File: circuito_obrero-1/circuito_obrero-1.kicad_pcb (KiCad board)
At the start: 2 copper layers, 13 parts, among them J1 Conn_01x03_Pin, J10 Conn_01x05, J2 Conn_01x03_Pin, J3 Conn_01x03_Pin, J4 Conn_01x03_Pin, J5 Conn_01x03_Pin, J6 Conn_01x03_Pin, J7 Conn_01x03_Pin, J8 Conn_01x03_Pin, J9 Conn_01x05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

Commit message: agregadas las resis al circuito
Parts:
- added R1: R, Resistor_THT:R_Axial_DIN0204_L3.6mm_D1.6mm_P5.08mm_Horizontal, F.Cu at (105.5, 89.1)
- added R10: R, Resistor_THT:R_Axial_DIN0204_L3.6mm_D1.6mm_P5.08mm_Horizontal, F.Cu at (113.5, 89.1)
- added R11: R, Resistor_THT:R_Axial_DIN0204_L3.6mm_D1.6mm_P5.08mm_Horizontal, F.Cu at (113.5, 92.2)
- added R12: R, Resistor_THT:R_Axial_DIN0204_L3.6mm_D1.6mm_P5.08mm_Horizontal, F.Cu at (113.5, 95.4)
- added R13: R, Resistor_THT:R_Axial_DIN0204_L3.6mm_D1.6mm_P5.08mm_Horizontal, F.Cu at (113.5, 98.5)
- added R14: R, Resistor_THT:R_Axial_DIN0204_L3.6mm_D1.6mm_P5.08mm_Horizontal, F.Cu at (113.5, 101.7)
- added R15: R, Resistor_THT:R_Axial_DIN0204_L3.6mm_D1.6mm_P5.08mm_Horizontal, F.Cu at (113.5, 104.8)
- added R16: R, Resistor_THT:R_Axial_DIN0204_L3.6mm_D1.6mm_P5.08mm_Horizontal, F.Cu at (113.5, 108.0)
- added R17: R, Resistor_THT:R_Axial_DIN0204_L3.6mm_D1.6mm_P5.08mm_Horizontal, F.Cu at (113.5, 111.1)
- added R18: R, Resistor_THT:R_Axial_DIN0204_L3.6mm_D1.6mm_P5.08mm_Horizontal, F.Cu at (113.5, 114.3)
- added R19: R, Resistor_THT:R_Axial_DIN0204_L3.6mm_D1.6mm_P5.08mm_Horizontal, F.Cu at (153.0, 85.5)
- added R2: R, Resistor_THT:R_Axial_DIN0204_L3.6mm_D1.6mm_P5.08mm_Horizontal, F.Cu at (105.5, 92.2)
- added R20: R, Resistor_THT:R_Axial_DIN0204_L3.6mm_D1.6mm_P5.08mm_Horizontal, F.Cu at (153.0, 81.5)
- added R21: R, Resistor_THT:R_Axial_DIN0204_L3.6mm_D1.6mm_P5.08mm_Horizontal, F.Cu at (121.5, 95.4)
- added R22: R, Resistor_THT:R_Axial_DIN0204_L3.6mm_D1.6mm_P5.08mm_Horizontal, F.Cu at (143.9, 77.5)
- added R23: R, Resistor_THT:R_Axial_DIN0204_L3.6mm_D1.6mm_P5.08mm_Horizontal, F.Cu at (121.5, 101.7)
- added R24: R, Resistor_THT:R_Axial_DIN0204_L3.6mm_D1.6mm_P5.08mm_Horizontal, F.Cu at (121.5, 104.8)
- added R3: R, Resistor_THT:R_Axial_DIN0204_L3.6mm_D1.6mm_P5.08mm_Horizontal, F.Cu at (105.5, 95.4)
- added R4: R, Resistor_THT:R_Axial_DIN0204_L3.6mm_D1.6mm_P5.08mm_Horizontal, F.Cu at (105.5, 98.5)
- added R5: R, Resistor_THT:R_Axial_DIN0204_L3.6mm_D1.6mm_P5.08mm_Horizontal, F.Cu at (105.5, 101.7)
- added R6: R, Resistor_THT:R_Axial_DIN0204_L3.6mm_D1.6mm_P5.08mm_Horizontal, F.Cu at (105.5, 104.8)
- added R7: R, Resistor_THT:R_Axial_DIN0204_L3.6mm_D1.6mm_P5.08mm_Horizontal, F.Cu at (105.5, 108.0)
- added R8: R, Resistor_THT:R_Axial_DIN0204_L3.6mm_D1.6mm_P5.08mm_Horizontal, F.Cu at (105.5, 111.1)
- added R9: R, Resistor_THT:R_Axial_DIN0204_L3.6mm_D1.6mm_P5.08mm_Horizontal, F.Cu at (105.5, 114.3)
- moved J10 116.3 mm to (193.0, 60.5), turned to -90 degrees
- moved J8 111.9 mm to (176.0, 71.0), turned to 90 degrees
- moved U3 54.4 mm to (152.4, 59.4)
- moved J9 40.1 mm to (40.0, 53.5), turned to -90 degrees
- moved U2 30.8 mm to (118.4, 49.8)
- moved U1 21.2 mm to (96.7, 51.9)
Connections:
- J10 pad 4: VCC -> GND
- J9 pad 4: VCC -> GND

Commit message: vcc funcional
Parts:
- moved J6 96.1 mm to (161.5, 74.3), turned to 180 degrees
- moved R24 74.9 mm to (190.4, 75.4), turned to 90 degrees
- moved J7 74.9 mm to (140.0, 88.8), turned to -90 degrees
- moved R23 70.8 mm to (187.3, 75.4), turned to 90 degrees
- moved J1 67.9 mm to (114.7, 93.8), turned to 90 degrees
- moved R21 62.7 mm to (181.0, 75.4), turned to 90 degrees
- moved R18 60.9 mm to (174.4, 113.3)
- moved J5 60.2 mm to (125.5, 73.8)
- moved J4 59.5 mm to (123.5, 52.0), turned to 180 degrees
- moved R9 58.3 mm to (106.5, 56.0), turned to 90 degrees
- moved R12 53.2 mm to (144.0, 51.8), turned to 90 degrees
- moved R17 51.4 mm to (164.4, 103.8)
- moved R16 50.0 mm to (146.5, 70.4), turned to 90 degrees
- moved R11 48.8 mm to (140.8, 51.8), turned to 90 degrees
- moved R10 44.4 mm to (137.7, 51.8), turned to 90 degrees
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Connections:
- J10 pad 4: GND -> VCC
- J9 pad 4: GND -> VCC
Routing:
- net (no net): track 0.00 -> 692.0 mm
- net GND: track 0.00 -> 10.1 mm

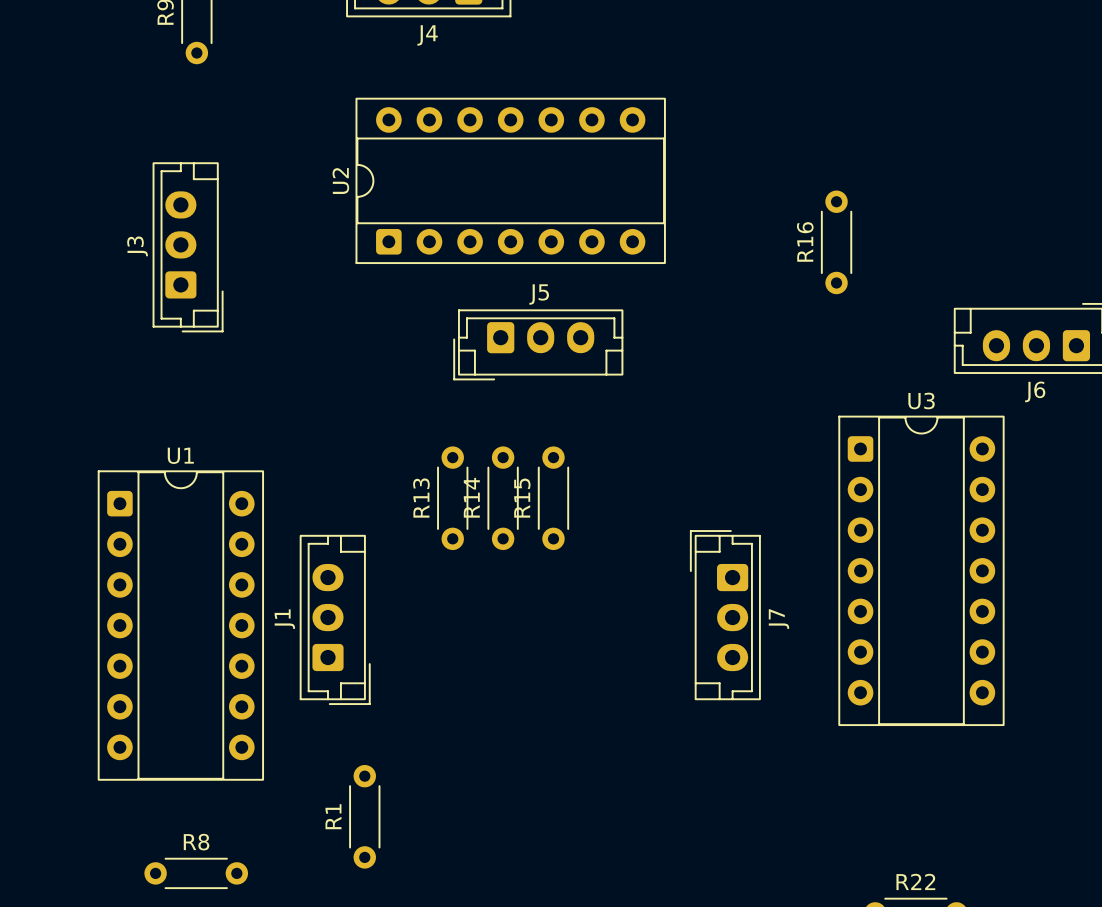
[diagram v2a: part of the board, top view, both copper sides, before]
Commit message: acomodando resistencias (revisar si es pull up o pull down el btn y los encoders)
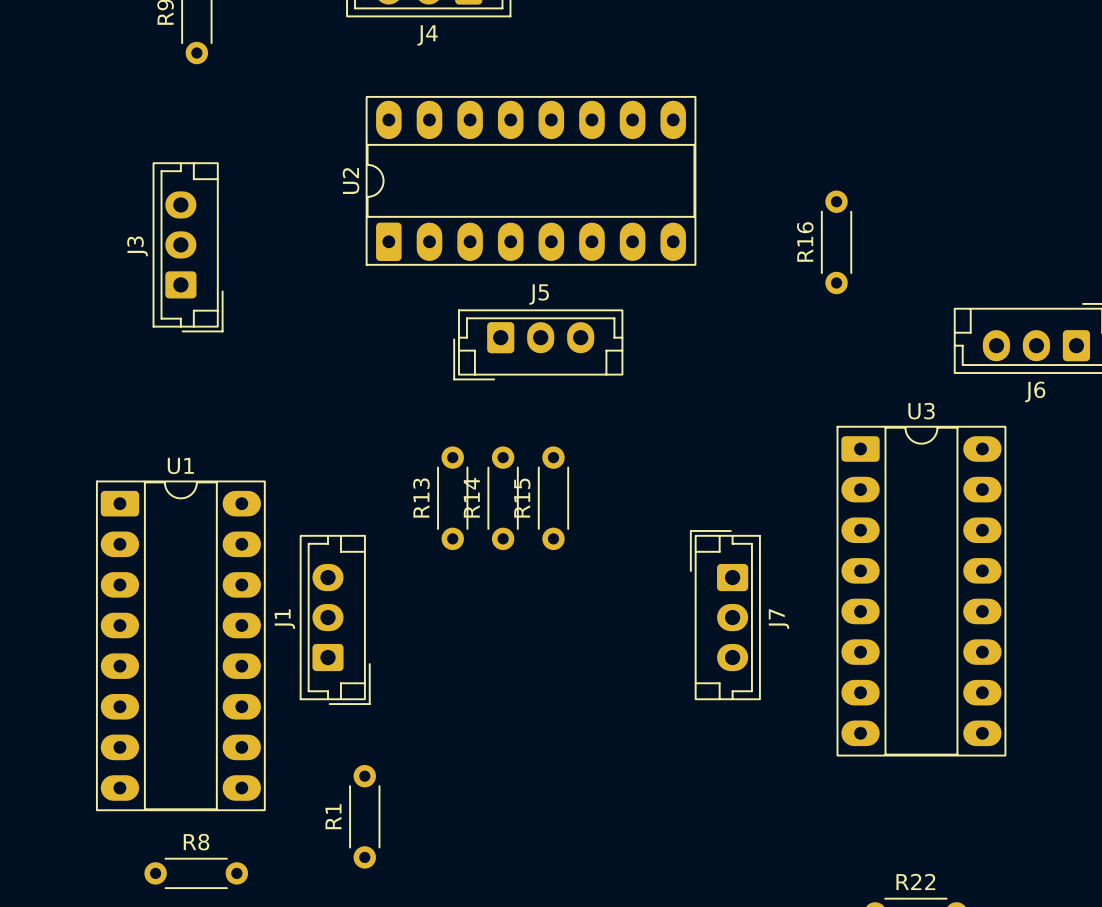
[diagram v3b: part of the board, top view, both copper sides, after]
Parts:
- U1, U2, U3: footprint Package_DIP:CERDIP-14_W7.62mm_SideBrazed_Socket -> Package_DIP:CERDIP-16_W7.62mm_SideBrazed_LongPads_Socket
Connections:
- R1 pad 1: GND -> VCC
- R10 pad 1: GND -> VCC
- R11 pad 1: Net-(J4-Pin_2) -> GND
- R11 pad 2: unconnected-(R11-Pad2) -> Net-(J4-Pin_2)
- R12 pad 1: GND -> VCC
- R13 pad 1: Net-(J5-Pin_1) -> VCC
- R13 pad 2: unconnected-(R13-Pad2) -> Net-(J5-Pin_1)
- R14 pad 1: Net-(J5-Pin_2) -> GND
- R14 pad 2: unconnected-(R14-Pad2) -> Net-(J5-Pin_2)
- R15 pad 2: unconnected-(R15-Pad2) -> VCC
- R16 pad 2: GND -> VCC
- R18 pad 1: GND -> VCC
- R19 pad 1: Net-(J7-Pin_3) -> VCC
- R19 pad 2: GND -> Net-(J6-Pin_1)
- R20 pad 1: Net-(J7-Pin_2) -> GND
- R20 pad 2: GND -> Net-(J6-Pin_2)
- R21 pad 1: GND -> VCC
- R21 pad 2: Net-(J7-Pin_1) -> Net-(J6-Pin_3)
- R22 pad 1: Net-(J6-Pin_3) -> VCC
- R22 pad 2: GND -> Net-(J7-Pin_1)
- R23 pad 1: Net-(J6-Pin_2) -> GND
- R23 pad 2: GND -> Net-(J7-Pin_2)
- R24 pad 1: GND -> VCC
- R24 pad 2: Net-(J6-Pin_1) -> Net-(J7-Pin_3)
- R3 pad 1: GND -> VCC
- R4 pad 1: GND -> VCC
- R6 pad 1: GND -> VCC
- R7 pad 1: GND -> VCC
- R8 pad 1: Net-(J3-Pin_2) -> GND
- R8 pad 2: GND -> Net-(J3-Pin_2)
- R9 pad 2: GND -> VCC

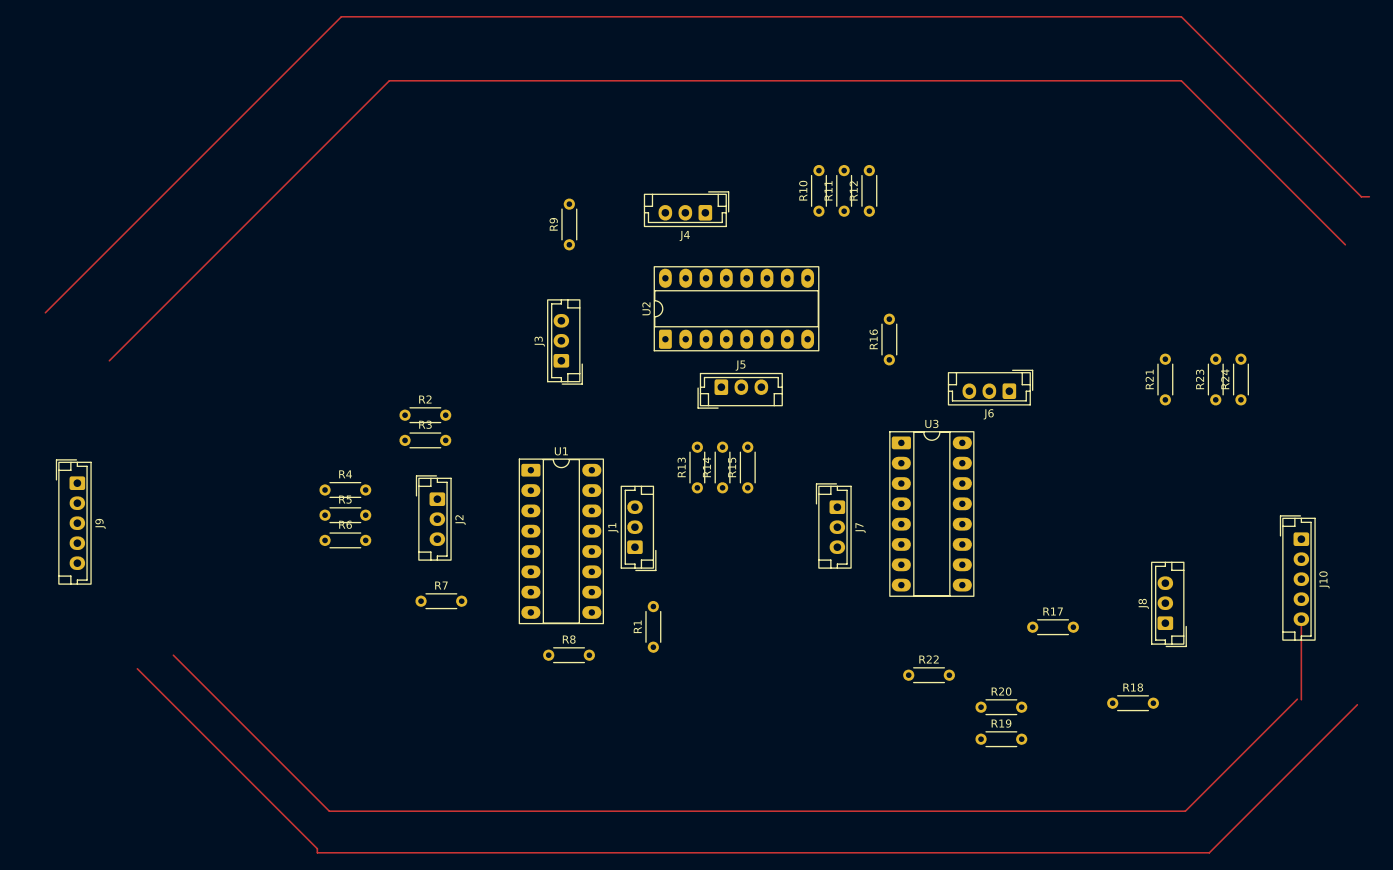
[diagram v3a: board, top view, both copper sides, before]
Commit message: revision de resistencias y otros elementos: falta ruteo en el circuito
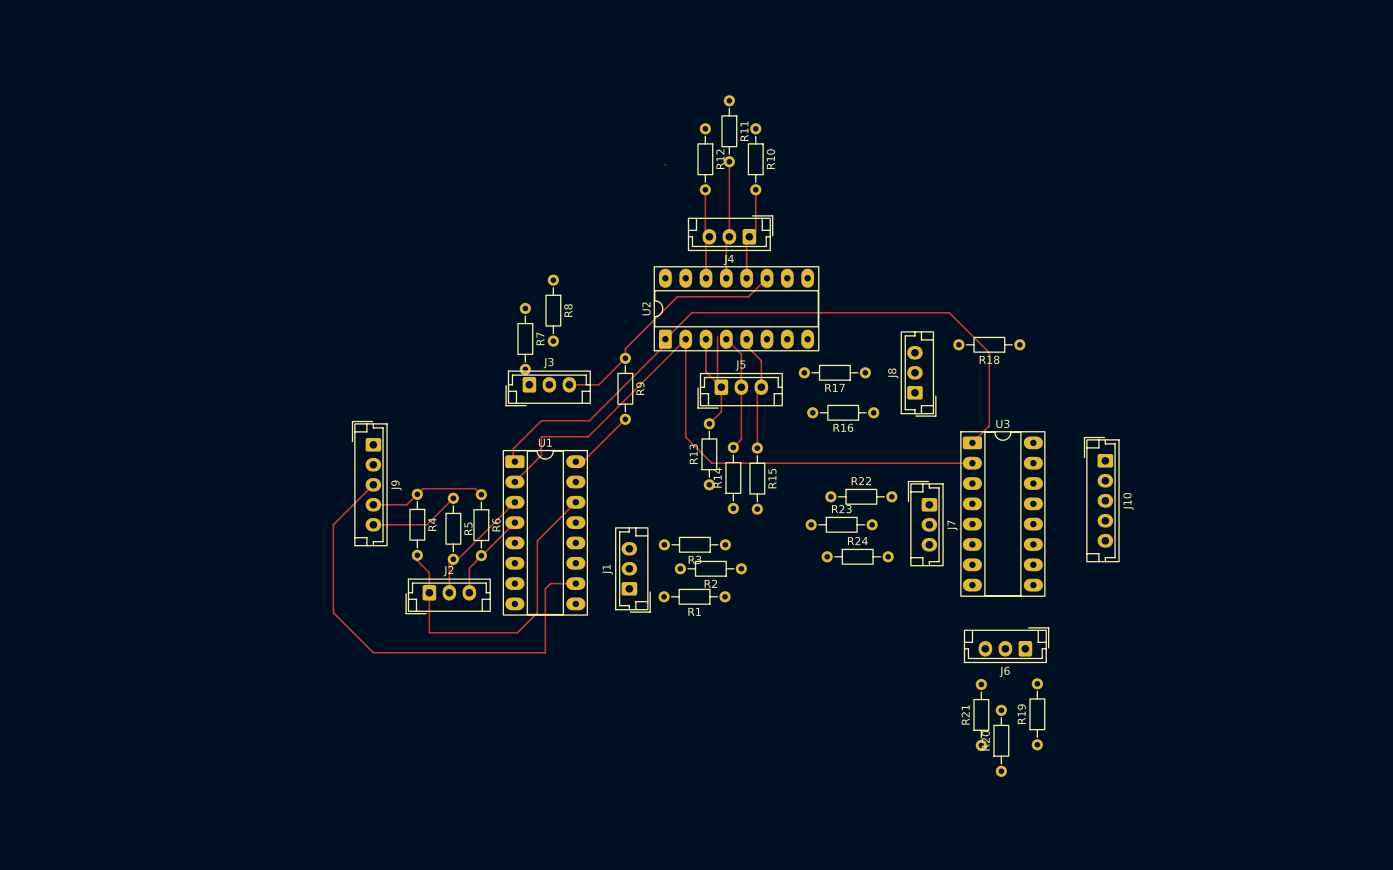
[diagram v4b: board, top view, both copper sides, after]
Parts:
- R1, R10, R11, R12, R13, R14, R15, R16, R17, R18, R19, R2, R20, R21, R22, R23, R24, R3, R4, R5, R6, R7, R8, R9: value R -> 10k; footprint Resistor_THT:R_Axial_DIN0204_L3.6mm_D1.6mm_P5.08mm_Horizontal -> Resistor_THT:R_Axial_DIN0204_L3.6mm_D1.6mm_P7.62mm_Horizontal
- moved R24 55.3 mm to (138.7, 95.0), turned to 0 degrees
- moved R23 52.9 mm to (136.7, 91.0), turned to 0 degrees
- moved R21 48.9 mm to (158.0, 118.6)
- moved R8 46.9 mm to (104.5, 60.4), turned to -90 degrees
- moved R18 46.3 mm to (162.8, 68.5), turned to 180 degrees
- moved R2 46.2 mm to (128.0, 96.5), turned to 180 degrees
- moved J8 42.5 mm to (149.7, 74.5)
- moved R3 42.1 mm to (126.0, 93.5), turned to 180 degrees
- moved R7 38.8 mm to (101.0, 64.0), turned to -90 degrees
- moved R17 38.1 mm to (143.5, 72.0), turned to 180 degrees
- moved J9 37.3 mm to (82.0, 81.0)
- moved J6 32.3 mm to (163.5, 106.5)
- moved J10 26.4 mm to (173.5, 83.0)
- moved R22 24.3 mm to (139.2, 87.5)
- moved R12 22.9 mm to (123.5, 41.5), turned to -90 degrees
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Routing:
- net (no net): track 692.0 -> 0.00 mm
- net Net-(J10-Pin_1): track 0.00 -> 82.9 mm
- net Net-(J10-Pin_2): track 0.00 -> 79.5 mm
- net Net-(J9-Pin_3): track 0.00 -> 58.7 mm
- net Net-(J2-Pin_1): track 0.00 -> 40.7 mm
- net Net-(J3-Pin_3): track 0.00 -> 30.9 mm
- net VCC: track 0.00 -> 23.0 mm
- net Net-(J5-Pin_1): track 0.00 -> 18.5 mm
- net Net-(J2-Pin_2): track 0.00 -> 16.2 mm
- net Net-(J4-Pin_2): track 0.00 -> 15.0 mm
- net Net-(J5-Pin_2): track 0.00 -> 14.7 mm
- net Net-(J5-Pin_3): track 0.00 -> 14.6 mm
- net Net-(J4-Pin_1): track 0.00 -> 11.6 mm
- net Net-(J2-Pin_3): track 0.00 -> 11.5 mm
- net Net-(J4-Pin_3): track 0.00 -> 11.5 mm
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
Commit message: preruteo: revisar y optimizar
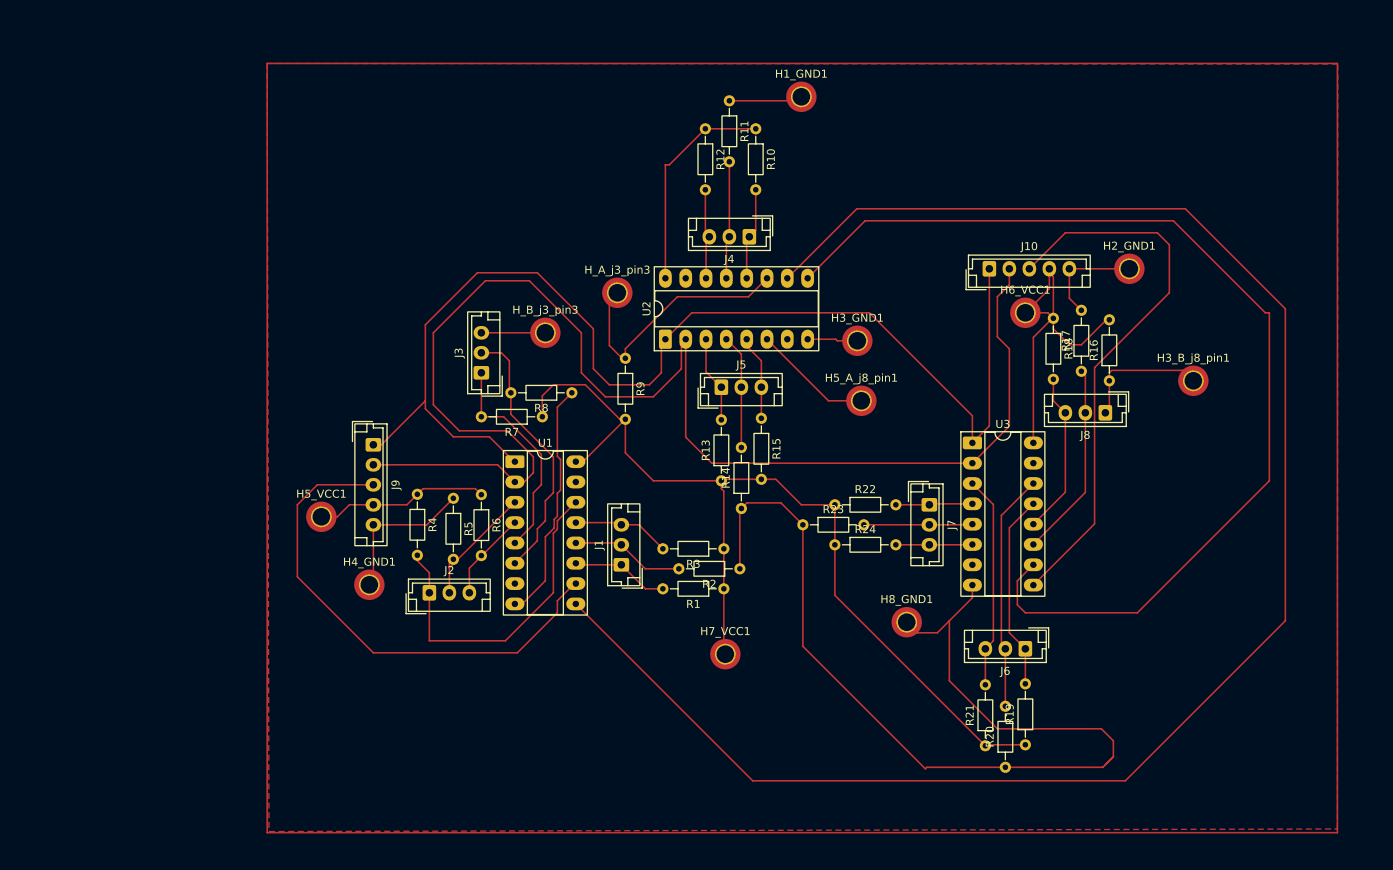
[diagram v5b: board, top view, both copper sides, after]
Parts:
- added H1_GND1: MountingHole_Pad, MountingHole:MountingHole_2.2mm_M2_DIN965_Pad_TopOnly, F.Cu at (135.5, 37.5)
- added H2_GND1: MountingHole_Pad, MountingHole:MountingHole_2.2mm_M2_DIN965_Pad_TopOnly, F.Cu at (176.5, 59.0)
- added H3_B_j8_pin1: MountingHole_Pad, MountingHole:MountingHole_2.2mm_M2_DIN965_Pad_TopOnly, F.Cu at (184.5, 73.0)
- added H3_GND1: MountingHole_Pad, MountingHole:MountingHole_2.2mm_M2_DIN965_Pad_TopOnly, F.Cu at (142.5, 68.0)
- added H4_GND1: MountingHole_Pad, MountingHole:MountingHole_2.2mm_M2_DIN965_Pad_TopOnly, F.Cu at (81.5, 98.5)
- added H5_A_j8_pin1: MountingHole_Pad, MountingHole:MountingHole_2.2mm_M2_DIN965_Pad_TopOnly, F.Cu at (143.0, 75.5)
- added H5_VCC1: MountingHole_Pad, MountingHole:MountingHole_2.2mm_M2_DIN965_Pad_TopOnly, F.Cu at (75.5, 90.0)
- added H6_VCC1: MountingHole_Pad, MountingHole:MountingHole_2.2mm_M2_DIN965_Pad_TopOnly, F.Cu at (163.5, 64.5)
- added H7_VCC1: MountingHole_Pad, MountingHole:MountingHole_2.2mm_M2_DIN965_Pad_TopOnly, F.Cu at (126.0, 107.2)
- added H8_GND1: MountingHole_Pad, MountingHole:MountingHole_2.2mm_M2_DIN965_Pad_TopOnly, F.Cu at (148.7, 103.2)
- added H_A_j3_pin3: MountingHole_Pad, MountingHole:MountingHole_2.2mm_M2_DIN965_Pad_TopOnly, F.Cu at (112.5, 62.0)
- added H_B_j3_pin3: MountingHole_Pad, MountingHole:MountingHole_2.2mm_M2_DIN965_Pad_TopOnly, F.Cu at (103.5, 67.0)
- moved R16 29.7 mm to (174.0, 73.0), turned to 90 degrees
- moved J10 28.0 mm to (159.0, 59.0), turned to 0 degrees
- moved R17 27.0 mm to (170.5, 71.8), turned to 90 degrees
- moved J8 23.9 mm to (173.5, 77.0), turned to 180 degrees
- moved R8 14.3 mm to (106.8, 74.5), turned to 180 degrees
- moved R7 13.7 mm to (103.1, 77.5), turned to 180 degrees
- moved J3 6.18 mm to (95.5, 72.0), turned to 90 degrees
- moved R18 5.34 mm to (167.0, 65.2), turned to -90 degrees
- moved R15 3.76 mm to (130.5, 77.7)
- moved J1 3.16 mm to (113.0, 96.0)
- moved R24 1.78 mm to (139.7, 93.5)
- moved R13 1.58 mm to (125.5, 85.5)
- moved R19 1.50 mm to (163.5, 118.5)
- moved R22 1.12 mm to (139.7, 88.5)
- moved R23 1.04 mm to (135.7, 91.0)
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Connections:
- R16 pad 1: Net-(J8-Pin_1) -> Net-(H3_B_j8_pin1-Pad1)
- R9 pad 1: Net-(J3-Pin_3) -> Net-(H_A_j3_pin3-Pad1)
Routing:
- net Net-(U1-Q7): track 0.00 -> 216.2 mm
- net VCC: track 23.0 -> 215.3 mm
- net GND: track 11.4 -> 202.5 mm
- net Net-(U2-Q7): track 0.00 -> 131.0 mm
- net Net-(J10-Pin_2): track 79.5 -> 172.6 mm
- net Net-(J10-Pin_3): track 0.00 -> 69.6 mm
- net Net-(J10-Pin_1): track 82.9 -> 150.2 mm
- net Net-(J3-Pin_2): track 0.00 -> 33.5 mm
- net Net-(J6-Pin_2): track 0.00 -> 29.7 mm
- net Net-(J3-Pin_1): track 0.00 -> 27.4 mm
- net Net-(J6-Pin_3): track 0.00 -> 26.7 mm
- net Net-(J6-Pin_1): track 0.00 -> 24.6 mm
- net Net-(J8-Pin_2): track 0.00 -> 24.5 mm
- net Net-(J8-Pin_3): track 0.00 -> 20.4 mm
- net Net-(J8-Pin_1): track 0.00 -> 19.2 mm
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- added copper zone on F.Cu, net GND
